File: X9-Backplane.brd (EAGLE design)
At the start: 122.1 x 89.3 mm, 12 parts

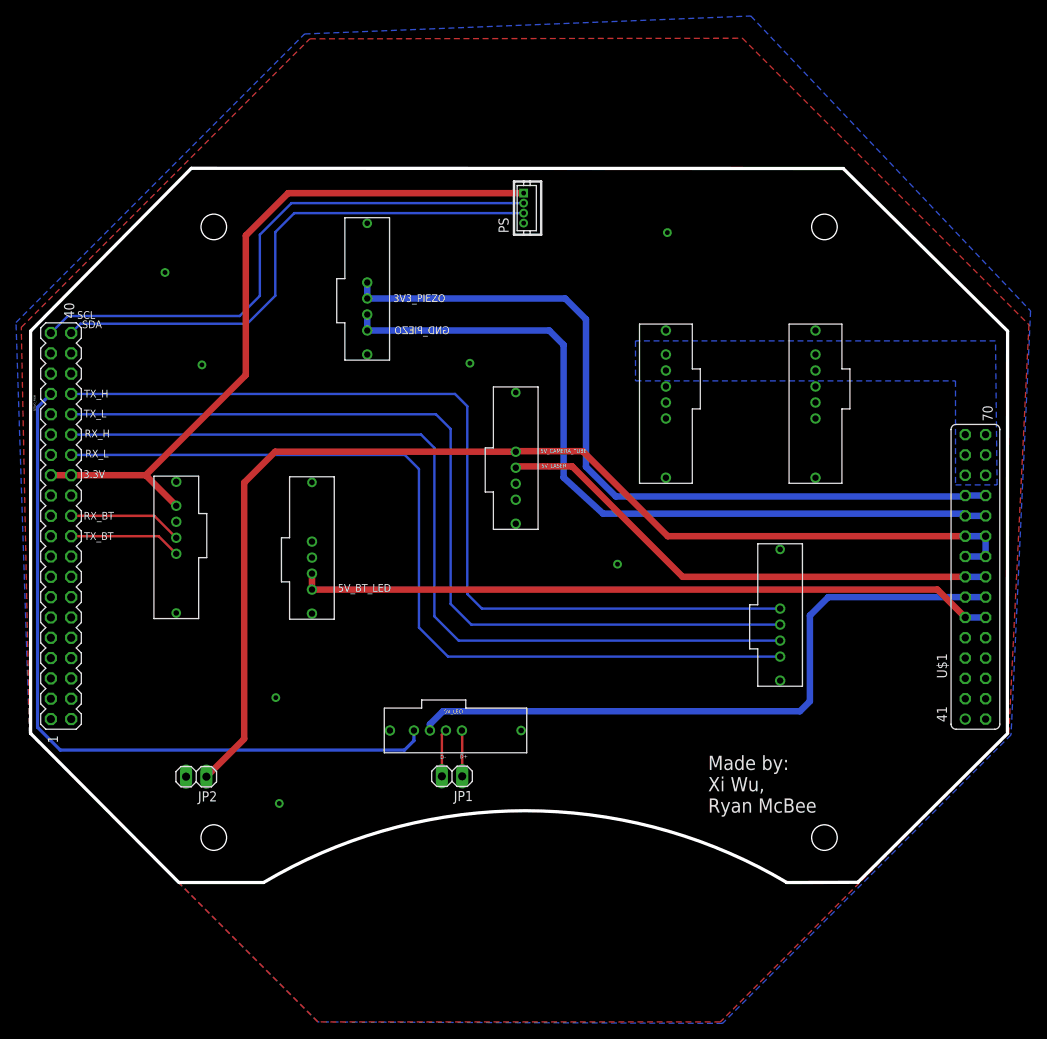
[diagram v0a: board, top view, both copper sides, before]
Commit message: reordered where the binders will be placed
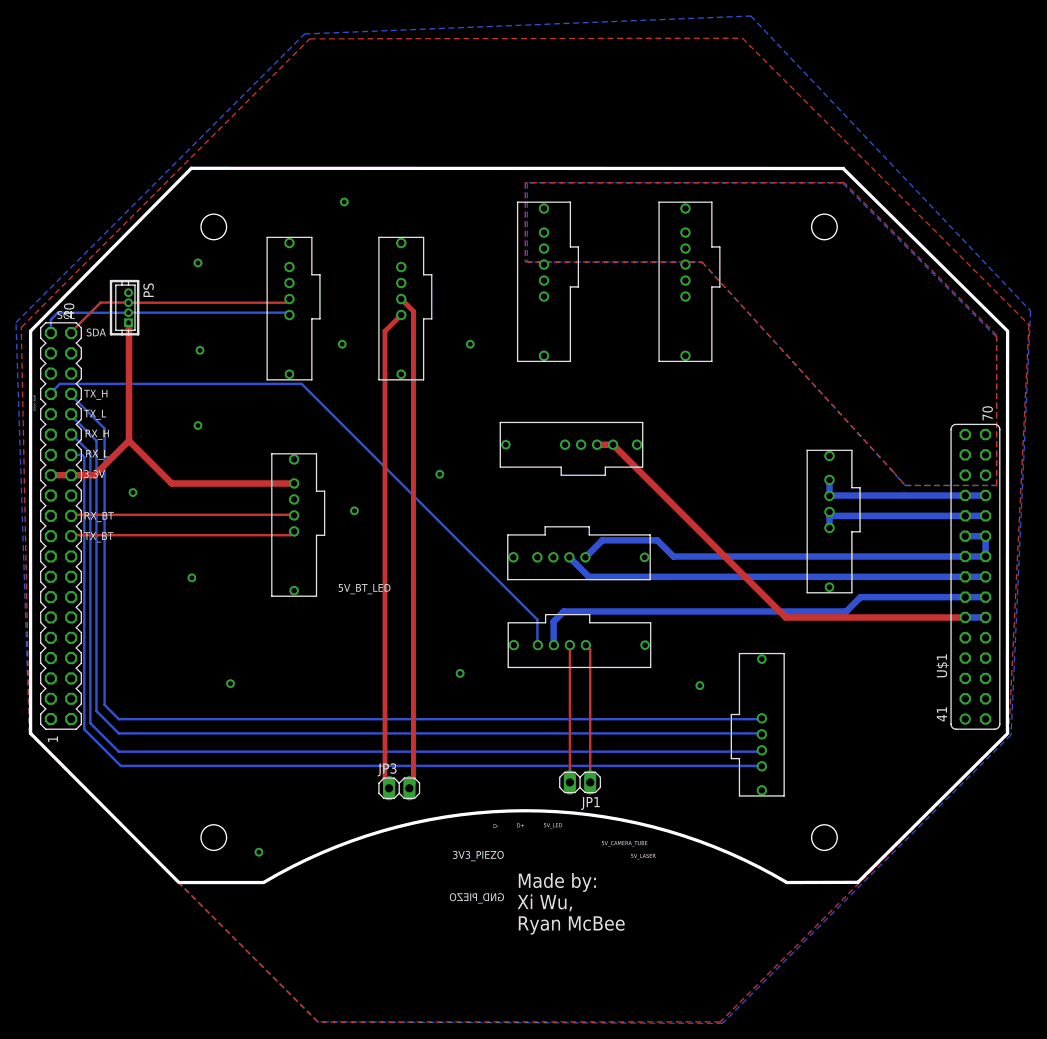
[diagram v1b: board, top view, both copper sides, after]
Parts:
- removed JP2: (no value), pinhead:1X02
- added JP3: (no value), pinhead:1X02
- added POW_COM_I2C, POW_COM_USB: T2I, BACKPLANE:T2I
- moved S_PIEZO 78.8 mm to (102.0, 29.5), turned to 90 degrees
- moved PS 50.9 mm to (11.6, 65.2), turned to 270 degrees
- moved CAMPOW 27.0 mm to (76.8, 36.7), turned to 180 degrees
- moved BT_POWER 26.4 mm to (58.1, 45.2), turned to 0 degrees
- moved POWER1 22.3 mm to (84.5, 78.2)
- moved POWER 21.6 mm to (66.9, 78.2)
- moved CAMDATA 18.8 mm to (76.9, 25.8)
- moved JP1 16.0 mm to (68.1, 5.81)
- moved BT_SIGNAL 15.0 mm to (35.1, 29.1)
- moved SC 13.9 mm to (88.0, 21.9)
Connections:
- net D+ renamed CAM_D+
- net D- renamed CAM_D-
- new net POW_D+: JP3.1, POW_COM_USB.1
- new net POW_D-: JP3.2, POW_COM_USB.2
- net 3V3_PIEZO: now also S_PIEZO.3, S_PIEZO.4; no longer S_PIEZO.1, S_PIEZO.2
- net 5V_CAMERA_TUBE: no longer JP2.1
- net GND: no longer JP2.2
- net GND_PIEZO: now also S_PIEZO.1, S_PIEZO.2; no longer S_PIEZO.3, S_PIEZO.4
- net SCL: now also POW_COM_I2C.1
- net SDA: now also POW_COM_I2C.2
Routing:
- net 5V_CAMERA_TUBE: track 142.5 -> 56.8 mm
- net 3V3_PIEZO: track 100.4 -> 21.6 mm
- net GND_PIEZO: track 98.5 -> 22.0 mm
- net POW_D-: track 0.00 -> 62.0 mm
- net POW_D+: track 0.00 -> 60.2 mm
- net 3.3V: track 89.3 -> 49.2 mm
- net SDA: track 67.4 -> 29.1 mm
- net SCL: track 70.3 -> 32.6 mm
- net 5V_BT_LED: track 87.6 -> 57.5 mm
- net 5V_LED: track 83.1 -> 58.2 mm
- net SERVO_PWM: track 92.3 -> 76.8 mm
- net TX_BT: track 14.0 -> 28.2 mm
- net RX_BT: track 14.3 -> 28.0 mm
- net RX_L: track 110.7 -> 122.4 mm
- net CAM_D+: track 5.74 -> 17.4 mm
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- added copper zone on layer 1, net +12V

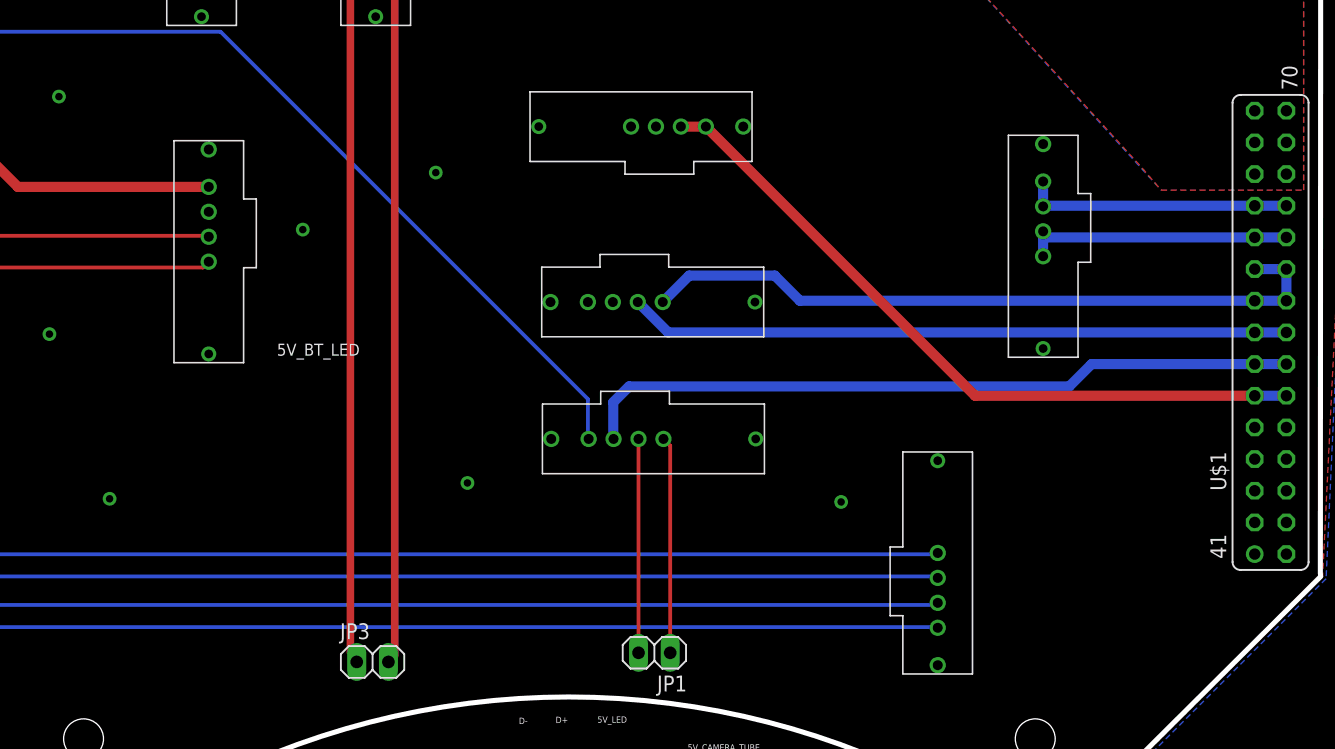
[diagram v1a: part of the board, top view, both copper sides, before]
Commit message: Moved around connector placement
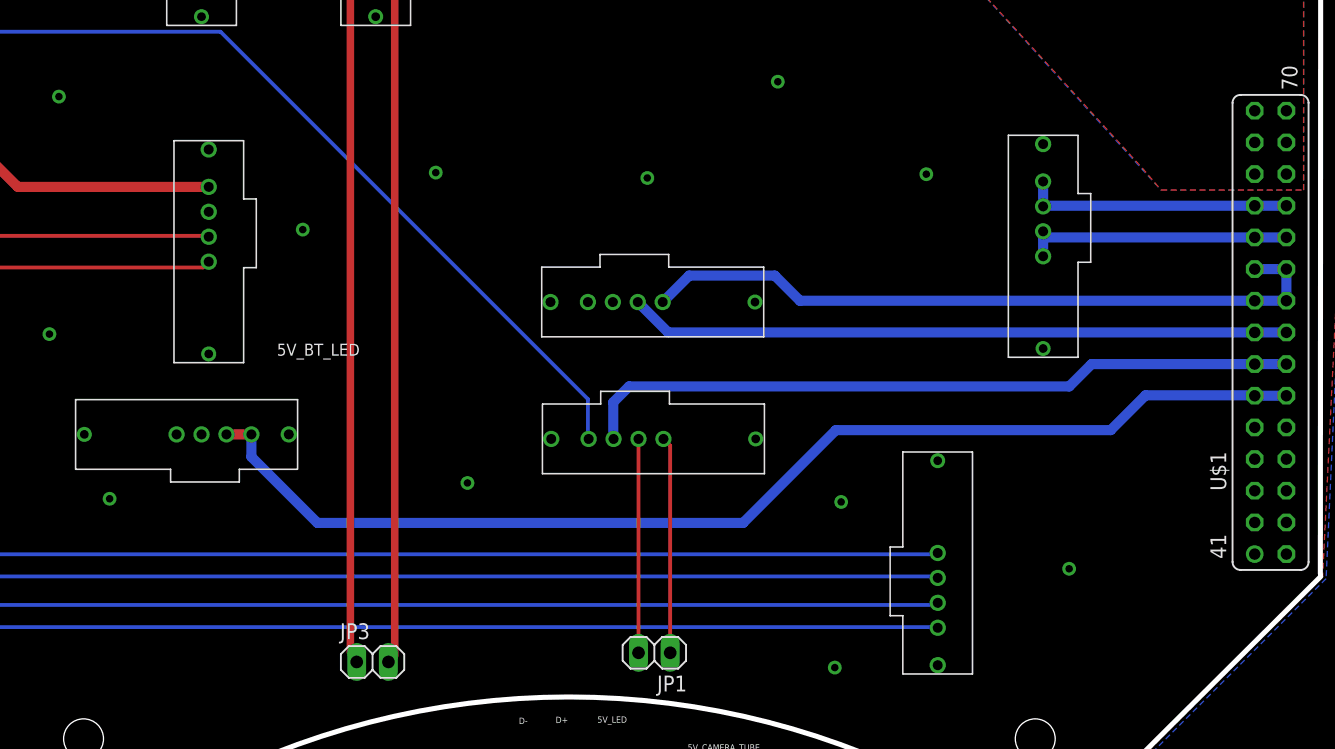
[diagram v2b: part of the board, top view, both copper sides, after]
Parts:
- moved BT_POWER 44.0 mm to (21.6, 20.5)
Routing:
- net 5V_BT_LED: track 57.5 -> 93.3 mm
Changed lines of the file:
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@@
 <setting verticaltext="up"/>
 </settings>
-<grid distance="10" unitdist="mil" unit="mil" style="lines" multiple="1" display="yes" altdistance="0.025" altunitdist="inch" altunit="inch"/>
+<grid distance="1" unitdist="mil" unit="mil" style="lines" multiple="1" display="yes" altdistance="0.025" altunitdist="inch" altunit="inch"/>
 <layers>
 <layer number="1" name="Top" color="4" fill="1" visible="yes" active="yes"/>
-<layer number="2" name="Route2" color="1" fill="3" visible="no" active="yes"/>
+<layer number="2" name="Route2" color="1" fill="3" visible="yes" active="yes"/>
 <layer number="3" name="Route3" color="4" fill="3" visible="no" active="yes"/>
 <layer number="4" name="Route4" color="1" fill="4" visible="no" active="yes"/>
@@
 <element name="POWER1" library="T2I5P" package="T2I5P" value="T2I5P" x="84.544" y="78.24" rot="R90"/>
 <element name="BT_SIGNAL" library="BACKPLANE" package="T2I" value="T2I" x="35.1246" y="29.083" rot="R90"/>
-<element name="BT_POWER" library="BACKPLANE" package="T2I" value="T2I" x="58.096" y="45.2194"/>
+<element name="BT_POWER" library="BACKPLANE" package="T2I" value="T2I" x="21.647" y="20.5306"/>
 <element name="U$1" library="backplane_to_shield_connector" package="20X2PIN" value="SHIELDCONNECTOR" x="57.8" y="40.4" smashed="yes">
 <attribute name="VALUE" x="6.619" y="22.62" size="1.27" layer="27" ratio="10" rot="R270"/>
@@
 <via x="83.047840625" y="17.91208125" extent="1-16" drill="0.6"/>
 <via x="12.181840625" y="42.04208125" extent="1-16" drill="0.6"/>
+<via x="67.503040625" y="43.89628125" extent="1-16" drill="0.6"/>
+<via x="77.967840625" y="51.61788125" extent="1-16" drill="0.6"/>
+<via x="89.880440625" y="44.20108125" extent="1-16" drill="0.6"/>
+<via x="101.335840625" y="12.55268125" extent="1-16" drill="0.6"/>
+<via x="82.539840625" y="4.62788125" extent="1-16" drill="0.6"/>
 </signal>
 <signal name="N$11">
@@
 <wire x1="118.76" y1="26.43" x2="116.22" y2="26.43" width="0.8128" layer="16"/>
 <contactref element="BT_POWER" pad="3"/>
-<wire x1="116.22" y1="26.43" x2="93.7854" y2="26.43" width="0.8128" layer="1"/>
-<wire x1="93.7854" y1="26.43" x2="72.196" y2="48.0194" width="0.8128" layer="1"/>
-<wire x1="72.196" y1="48.0194" x2="70.196" y2="48.0194" width="0.8128" layer="1"/>
+<wire x1="35.747" y1="23.3306" x2="33.747" y2="23.3306" width="0.8128" layer="1"/>
+<wire x1="35.747" y1="23.3306" x2="35.747" y2="21.53" width="0.8128" layer="16"/>
+<wire x1="35.747" y1="21.53" x2="41.0464" y2="16.2306" width="0.8128" layer="16"/>
+<wire x1="41.0464" y1="16.2306" x2="75.184" y2="16.2306" width="0.8128" layer="16"/>
+<wire x1="75.184" y1="16.2306" x2="82.6262" y2="23.6728" width="0.8128" layer="16"/>
+<wire x1="82.6262" y1="23.6728" x2="104.6734" y2="23.6728" width="0.8128" layer="16"/>
+<wire x1="104.6734" y1="23.6728" x2="107.4674" y2="26.4668" width="0.8128" layer="16"/>
+<wire x1="107.4674" y1="26.4668" x2="116.1832" y2="26.4668" width="0.8128" layer="16"/>
+<wire x1="116.1832" y1="26.4668" x2="116.22" y2="26.43" width="0.8128" layer="16"/>
 </signal>
 <signal name="RX_BT">

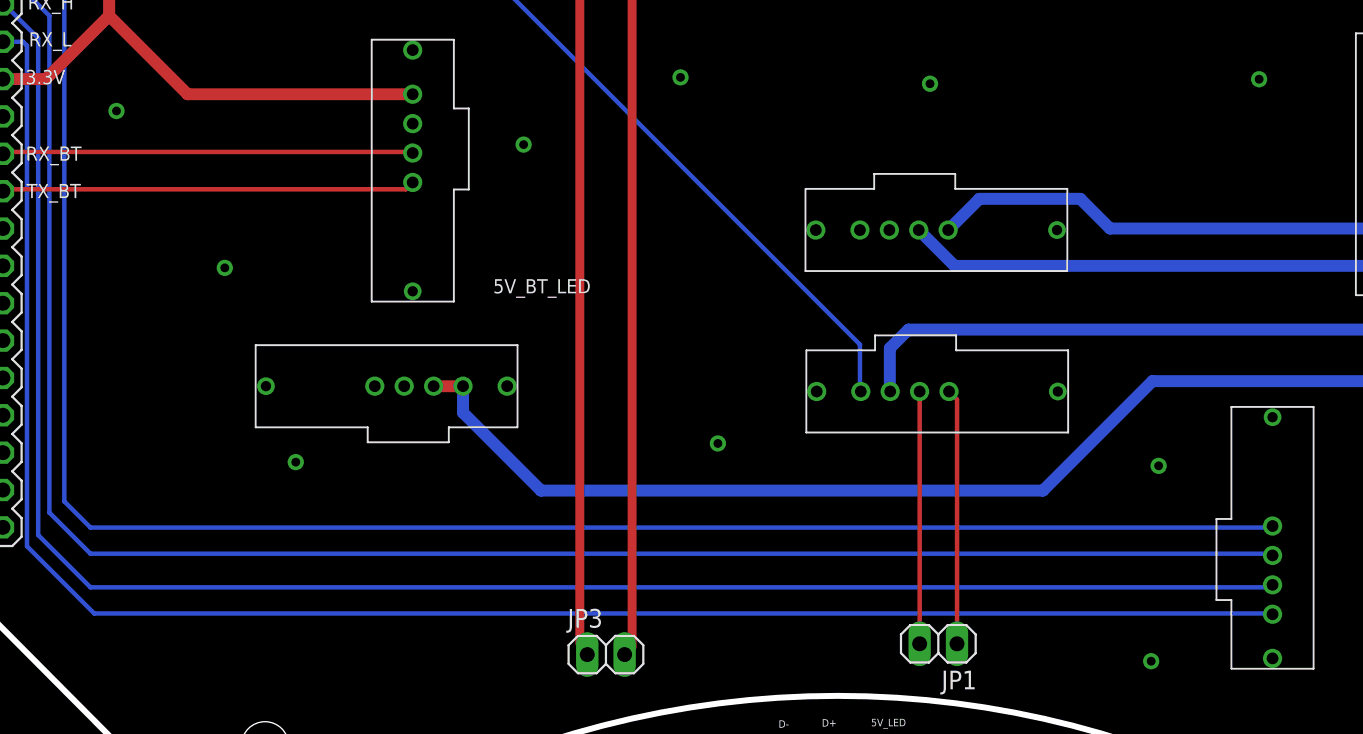
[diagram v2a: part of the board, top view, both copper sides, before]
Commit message: Added extra connector for bluetooth just in case
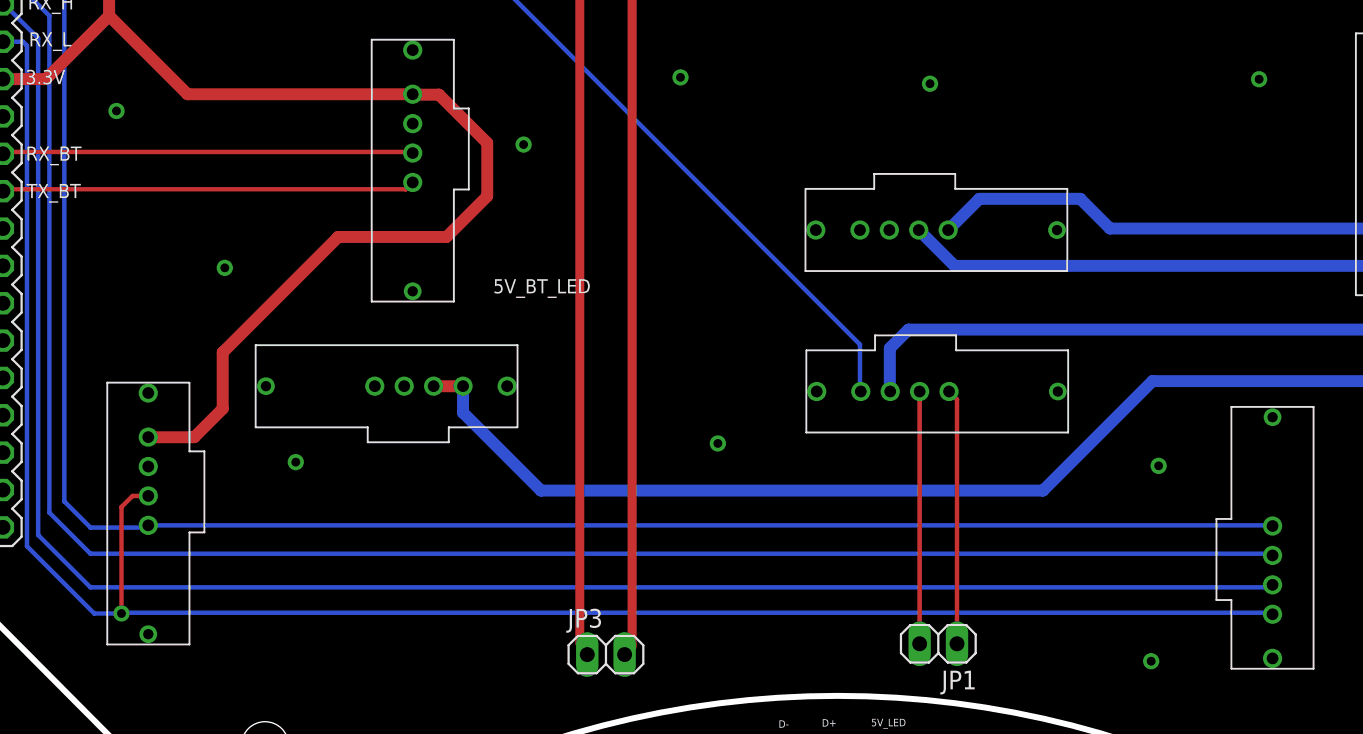
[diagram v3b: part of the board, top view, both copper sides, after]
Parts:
- added SC1: T2I, BACKPLANE:T2I
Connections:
- net 3.3V: now also SC1.4
- net GND: now also SC1.3
- net RX_L: now also SC1.2
- net TX_H: now also SC1.1
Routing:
- net 3.3V: track 49.2 -> 91.3 mm
- net RX_L: track 122.4 -> 131.9 mm, vias 0 -> 1
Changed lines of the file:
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@@
 <layers>
 <layer number="1" name="Top" color="4" fill="1" visible="yes" active="yes"/>
-<layer number="2" name="Route2" color="1" fill="3" visible="yes" active="yes"/>
+<layer number="2" name="Route2" color="1" fill="3" visible="no" active="yes"/>
 <layer number="3" name="Route3" color="4" fill="3" visible="no" active="yes"/>
 <layer number="4" name="Route4" color="1" fill="4" visible="no" active="yes"/>
@@
 <element name="JP3" library="pinhead" package="1X02" value="" x="45.466" y="5.08"/>
 <element name="POW_COM_I2C" library="BACKPLANE" package="T2I" value="T2I" x="34.544" y="56.134" rot="R90"/>
+<element name="SC1" library="BACKPLANE" package="T2I" value="T2I" x="17.145" y="5.7658" rot="R90"/>
 </elements>
 <signals>
@@
 <via x="101.335840625" y="12.55268125" extent="1-16" drill="0.6"/>
 <via x="82.539840625" y="4.62788125" extent="1-16" drill="0.6"/>
+<contactref element="SC1" pad="3"/>
 </signal>
 <signal name="N$11">
@@
 <wire x1="17.018" y1="43.18" x2="32.3216" y2="43.18" width="0.8128" layer="1"/>
 <wire x1="32.3216" y1="43.18" x2="32.3246" y2="43.183" width="0.8128" layer="1"/>
+<wire x1="19.4056" y1="25.6286" x2="27.2542" y2="33.4772" width="0.8128" layer="1"/>
+<wire x1="27.2542" y1="33.4772" x2="34.6202" y2="33.4772" width="0.8128" layer="1"/>
+<wire x1="34.6202" y1="33.4772" x2="37.3888" y2="36.2458" width="0.8128" layer="1"/>
+<wire x1="37.3888" y1="36.2458" x2="37.3888" y2="39.878" width="0.8128" layer="1"/>
+<wire x1="37.3888" y1="39.878" x2="34.1122" y2="43.1546" width="0.8128" layer="1"/>
+<wire x1="34.1122" y1="43.1546" x2="32.353" y2="43.1546" width="0.8128" layer="1"/>
+<wire x1="32.353" y1="43.1546" x2="32.3246" y2="43.183" width="0.8128" layer="1"/>
+<contactref element="SC1" pad="4"/>
+<wire x1="19.4056" y1="25.6286" x2="19.4056" y2="21.7932" width="0.8128" layer="1"/>
+<wire x1="19.4056" y1="21.7932" x2="17.4752" y2="19.8628" width="0.8128" layer="1"/>
+<wire x1="17.4752" y1="19.8628" x2="14.348" y2="19.8628" width="0.8128" layer="1"/>
+<wire x1="14.348" y1="19.8628" x2="14.345" y2="19.8658" width="0.8128" layer="1"/>
 </signal>
 <signal name="TX_H">
@@
 <wire x1="8.636" y1="50.038" x2="8.636" y2="15.494" width="0.3048" layer="16"/>
 <wire x1="8.636" y1="15.494" x2="10.414" y2="13.716" width="0.3048" layer="16"/>
-<wire x1="10.414" y1="13.716" x2="90.6908" y2="13.716" width="0.3048" layer="16"/>
-<wire x1="90.6908" y1="13.716" x2="90.795" y2="13.8202" width="0.3048" layer="16"/>
+<contactref element="SC1" pad="1"/>
+<wire x1="10.414" y1="13.716" x2="14.1952" y2="13.716" width="0.3048" layer="16"/>
+<wire x1="14.1952" y1="13.716" x2="14.345" y2="13.8658" width="0.3048" layer="16"/>
+<wire x1="14.345" y1="13.8658" x2="90.7494" y2="13.8658" width="0.3048" layer="16"/>
+<wire x1="90.7494" y1="13.8658" x2="90.795" y2="13.8202" width="0.3048" layer="16"/>
 </signal>
 <signal name="3V3_PIEZO">
@@
 <wire x1="7.62" y1="48.514" x2="7.62" y2="14.732" width="0.3048" layer="16"/>
 <wire x1="7.62" y1="14.732" x2="10.414" y2="11.938" width="0.3048" layer="16"/>
+<wire x1="90.7604" y1="11.7856" x2="90.795" y2="11.8202" width="0.3048" layer="16"/>
 <wire x1="10.414" y1="11.938" x2="90.6772" y2="11.938" width="0.3048" layer="16"/>
 <wire x1="90.6772" y1="11.938" x2="90.795" y2="11.8202" width="0.3048" layer="16"/>
@@
 <wire x1="6.858" y1="46.99" x2="6.858" y2="13.208" width="0.3048" layer="16"/>
 <wire x1="6.858" y1="13.208" x2="10.414" y2="9.652" width="0.3048" layer="16"/>
+<wire x1="90.76" y1="9.8552" x2="90.795" y2="9.8202" width="0.3048" layer="16"/>
 <wire x1="10.414" y1="9.652" x2="90.6268" y2="9.652" width="0.3048" layer="16"/>
 <wire x1="90.6268" y1="9.652" x2="90.795" y2="9.8202" width="0.3048" layer="16"/>
@@
 <wire x1="6.096" y1="46.482" x2="6.096" y2="12.446" width="0.3048" layer="16"/>
 <wire x1="6.096" y1="12.446" x2="10.668" y2="7.874" width="0.3048" layer="16"/>
-<wire x1="10.668" y1="7.874" x2="90.7412" y2="7.874" width="0.3048" layer="16"/>
 <wire x1="90.7412" y1="7.874" x2="90.795" y2="7.8202" width="0.3048" layer="16"/>
+<wire x1="90.6904" y1="7.9248" x2="90.795" y2="7.8202" width="0.3048" layer="16"/>
+<contactref element="SC1" pad="2"/>
+<wire x1="14.345" y1="15.8658" x2="13.275" y2="15.8658" width="0.3048" layer="1"/>
+<wire x1="13.275" y1="15.8658" x2="12.5222" y2="15.113" width="0.3048" layer="1"/>
+<wire x1="10.668" y1="7.874" x2="12.5222" y2="7.874" width="0.3048" layer="16"/>
+<via x="12.5222" y="7.874" extent="1-16" drill="0.6"/>
+<wire x1="12.5222" y1="7.874" x2="12.5222" y2="15.113" width="0.3048" layer="1"/>
+<wire x1="90.6904" y1="7.9248" x2="12.573" y2="7.9248" width="0.3048" layer="16"/>
+<wire x1="12.573" y1="7.9248" x2="12.5222" y2="7.874" width="0.3048" layer="16"/>
 </signal>
 <signal name="GND_PIEZO">
